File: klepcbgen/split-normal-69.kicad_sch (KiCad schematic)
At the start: 159 parts, among them J1 USB_B_Micro, J2 Conn_02x03_Odd_Even, K0 Esc, K1 !,1,,F1, K10 ),0,,F10, K11 _,-,,F11, K12 +,=,,F12, K13 Backspace, K14 Delete,Insert, K15 Tab, K16 Q, K17 W, K18 E, K19 R, K2 @,2,,F2, K20 T, K21 Y, K22 U, K23 I, K24 O, K25 P, K26 {,[, K27 },], K28 |,\, K29 ~~,`, K3 #,3,,F3, K30 Caps Lock, K31 A, K32 S, K33 D, K34 F, K35 G, K36 H, K37 J, K38 K, K39 L, K4 $,4,,F4, K40 :,;, K41 ",', K42 Enter, K43 Home,PgUp, K44 Shift, K45 Z, K46 X, K47 C, K48 V, K49 B, K5 %,5,,F5, K50 N, K51 M, K52 <,,, K53 >,., K54 ?,/, K55 Shift, K56 ↑, K57 End,PgDn, K58 Ctrl, K59 Win, K6 ^,6,,F6, K60 Alt, K61 Blank, K62 Blank, K63 Alt, K64 Fn, K65 Ctrl, K66 ←, K67 ↓, K68 →, K7 &,7,,F7, K8 *,8,,F8, K9 (,9,,F9, SW1 RESET_SW, U1 ATmega32U4-AU, Y1 Crystal

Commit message: update
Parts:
- H1, H2, H3, H4: footprint MountingHole:MountingHole_3.2mm_M3_DIN965 -> MountingHole:MountingHole_3.2mm_M3
- K61, K62: value Blank -> Space
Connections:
- net Col_0 renamed COL0
- net Col_1 renamed COL1
- net Col_10 renamed COL10
- net Col_11 renamed COL11
- net Col_12 renamed COL12
- net Col_13 renamed COL13
- net Col_14 renamed COL14
- net Col_15: no longer names the net of U1.40 (PF1)
- net Col_16: no longer names the net of U1.41 (PF0)
- net Col_17: no longer names the net of U1.1 (PE6)
- net Col_2 renamed COL2
- net Col_3 renamed COL3
- net Col_4 renamed COL4
- net Col_5 renamed COL5
- net Col_6 renamed COL6
- net Col_7 renamed COL7
- net Col_8 renamed COL8
- net Col_9 renamed COL9
- net Row_0 renamed ROW0
- net Row_1 renamed ROW1
- net Row_2 renamed ROW2
- net Row_3 renamed ROW3
- net Row_4 renamed ROW4
- net Row_5: no longer names the net of U1.27 (PD7)
- net Row_6: no longer names the net of U1.26 (PD6)
- no-connect marks 2 -> 7

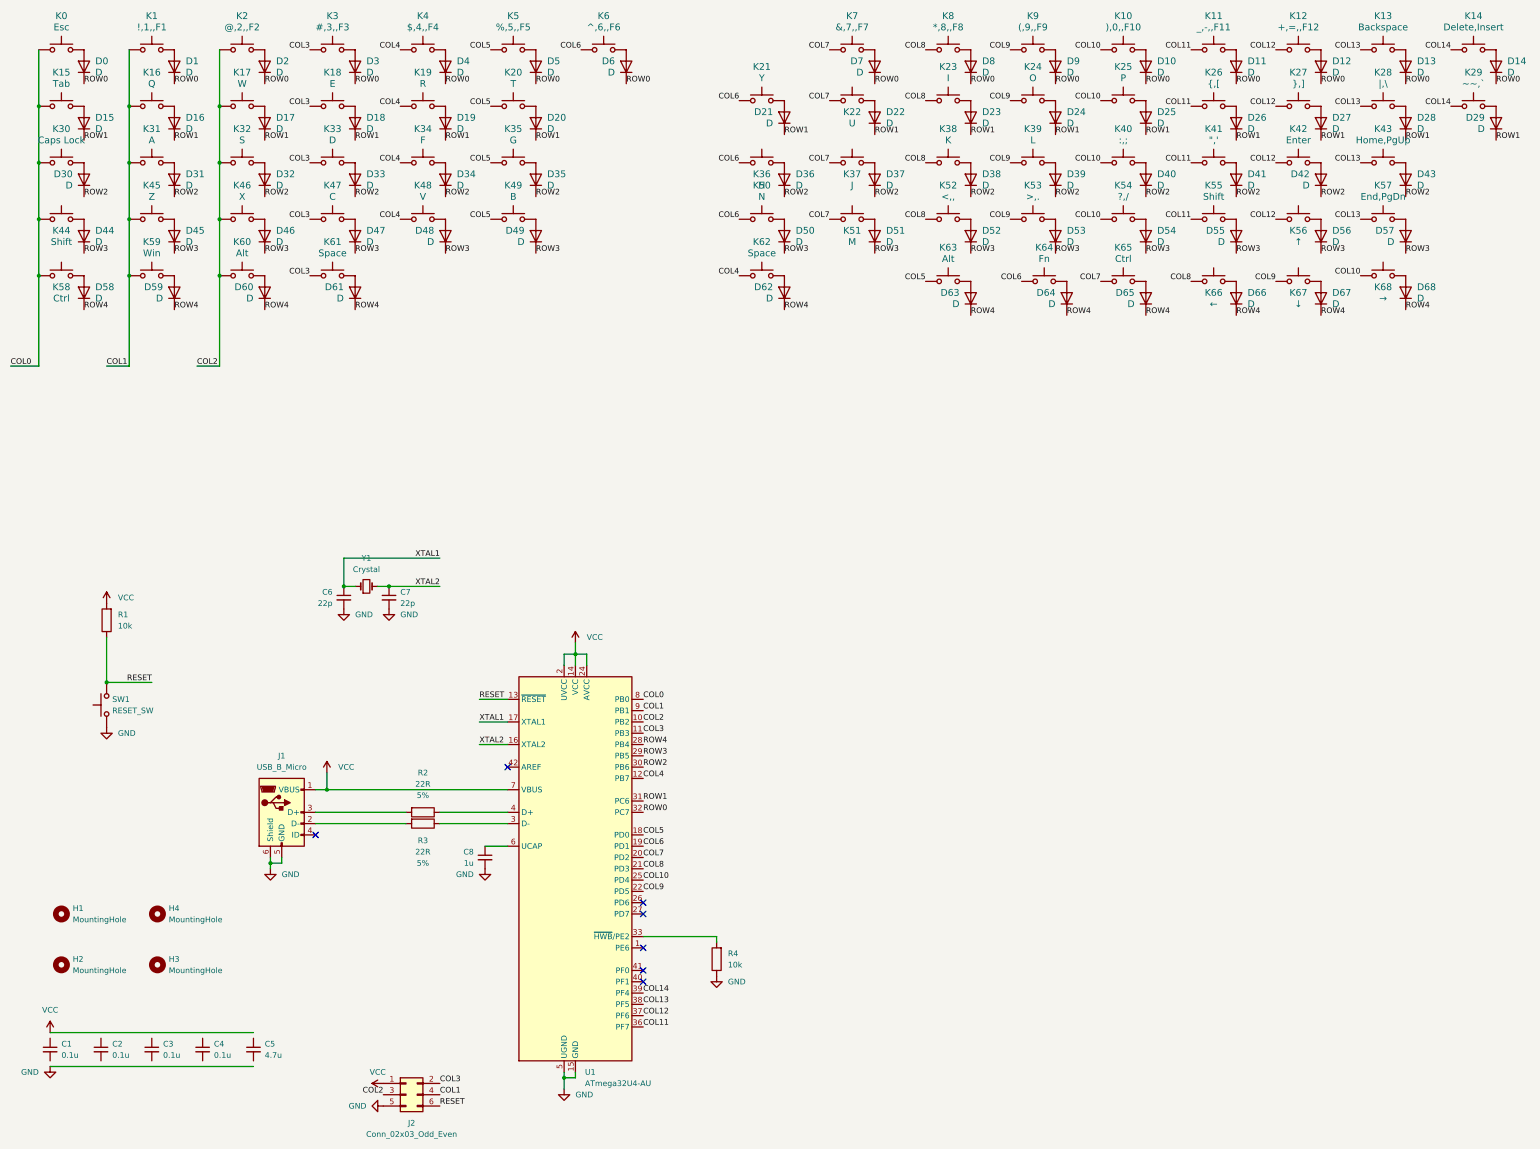
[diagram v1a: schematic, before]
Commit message: Continued development. Fixed the keyboard connections. Trying to figure out how to connect them together.
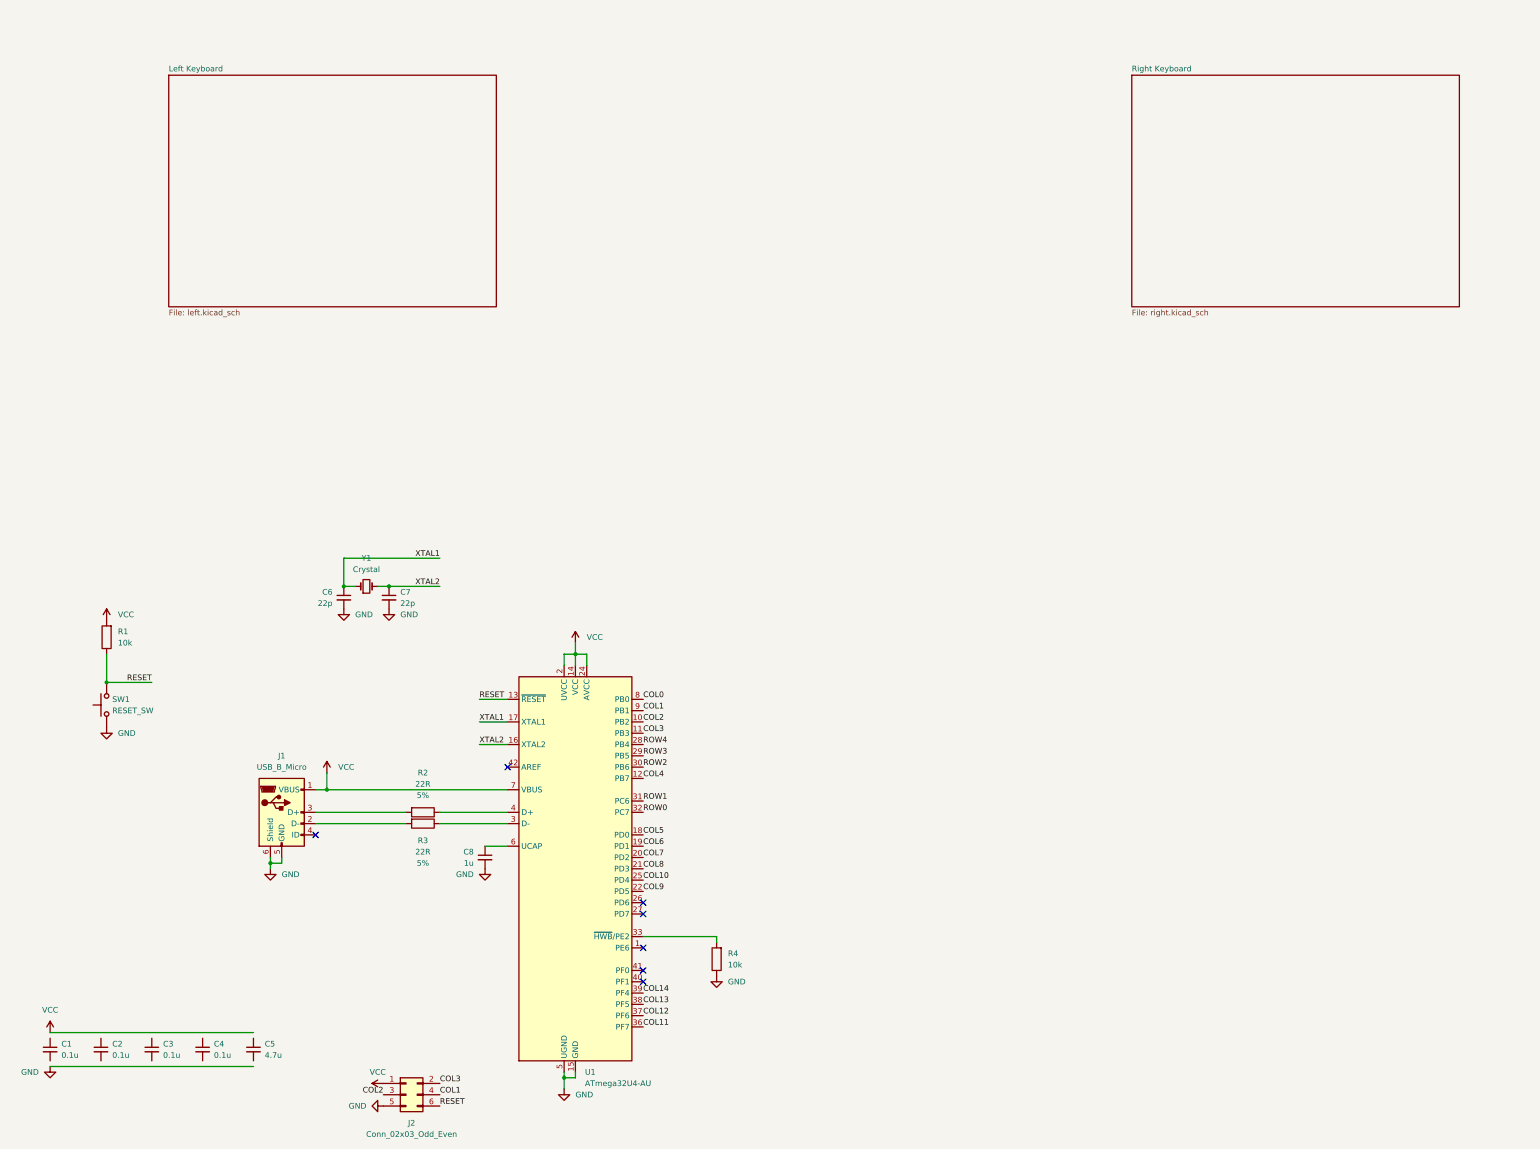
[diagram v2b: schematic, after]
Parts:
- removed D0, D1, D10, D11, D12, D13, D14, D15, D16, D17, D18, D19, D2, D20, D21, D22, D23, D24, D25, D26, D27, D28, D29, D3, D30, D31, D32, D33, D34, D35, D36, D37, D38, D39, D4, D40, D41, D42, D43, D44, D45, D46, D47, D48, D49, D5, D50, D51, D52, D53, D54, D55, D56, D57, D58, D59, D6, D60, D61, D62, D63, D64, D65, D66, D67, D68, D7, D8, D9: D, Diode_SMD:D_0805_2012Metric_Pad1.15x1.40mm_HandSolder, symbol Device:D
- removed H1, H2, H3, H4: MountingHole, MountingHole:MountingHole_3.2mm_M3, symbol Mechanical:MountingHole
- removed K0: Esc, Button_Switch_Keyboard:SW_Cherry_MX_1.00u_PCB, symbol Switch:SW_Push
- removed K1: !,1,,F1, Button_Switch_Keyboard:SW_Cherry_MX_1.00u_PCB, symbol Switch:SW_Push
- removed K10: ),0,,F10, Button_Switch_Keyboard:SW_Cherry_MX_1.00u_PCB, symbol Switch:SW_Push
- removed K11: _,-,,F11, Button_Switch_Keyboard:SW_Cherry_MX_1.00u_PCB, symbol Switch:SW_Push
- removed K12: +,=,,F12, Button_Switch_Keyboard:SW_Cherry_MX_1.00u_PCB, symbol Switch:SW_Push
- removed K13: Backspace, Button_Switch_Keyboard:SW_Cherry_MX_2.00u_PCB, symbol Switch:SW_Push
- removed K14: Delete,Insert, Button_Switch_Keyboard:SW_Cherry_MX_1.00u_PCB, symbol Switch:SW_Push
- removed K15: Tab, Button_Switch_Keyboard:SW_Cherry_MX_1.50u_PCB, symbol Switch:SW_Push
- removed K16: Q, Button_Switch_Keyboard:SW_Cherry_MX_1.00u_PCB, symbol Switch:SW_Push
- removed K17: W, Button_Switch_Keyboard:SW_Cherry_MX_1.00u_PCB, symbol Switch:SW_Push
- removed K18: E, Button_Switch_Keyboard:SW_Cherry_MX_1.00u_PCB, symbol Switch:SW_Push
- removed K19: R, Button_Switch_Keyboard:SW_Cherry_MX_1.00u_PCB, symbol Switch:SW_Push
- removed K2: @,2,,F2, Button_Switch_Keyboard:SW_Cherry_MX_1.00u_PCB, symbol Switch:SW_Push
- removed K20: T, Button_Switch_Keyboard:SW_Cherry_MX_1.00u_PCB, symbol Switch:SW_Push
- removed K21: Y, Button_Switch_Keyboard:SW_Cherry_MX_1.00u_PCB, symbol Switch:SW_Push
- removed K22: U, Button_Switch_Keyboard:SW_Cherry_MX_1.00u_PCB, symbol Switch:SW_Push
- removed K23: I, Button_Switch_Keyboard:SW_Cherry_MX_1.00u_PCB, symbol Switch:SW_Push
- removed K24: O, Button_Switch_Keyboard:SW_Cherry_MX_1.00u_PCB, symbol Switch:SW_Push
- removed K25: P, Button_Switch_Keyboard:SW_Cherry_MX_1.00u_PCB, symbol Switch:SW_Push
- removed K26: {,[, Button_Switch_Keyboard:SW_Cherry_MX_1.00u_PCB, symbol Switch:SW_Push
- removed K27: },], Button_Switch_Keyboard:SW_Cherry_MX_1.00u_PCB, symbol Switch:SW_Push
- removed K28: |,\, Button_Switch_Keyboard:SW_Cherry_MX_1.50u_PCB, symbol Switch:SW_Push
- removed K29: ~~,`, Button_Switch_Keyboard:SW_Cherry_MX_1.00u_PCB, symbol Switch:SW_Push
- removed K3: #,3,,F3, Button_Switch_Keyboard:SW_Cherry_MX_1.00u_PCB, symbol Switch:SW_Push
- removed K30: Caps Lock, Button_Switch_Keyboard:SW_Cherry_MX_1.75u_PCB, symbol Switch:SW_Push
- removed K31: A, Button_Switch_Keyboard:SW_Cherry_MX_1.00u_PCB, symbol Switch:SW_Push
- removed K32: S, Button_Switch_Keyboard:SW_Cherry_MX_1.00u_PCB, symbol Switch:SW_Push
- removed K33: D, Button_Switch_Keyboard:SW_Cherry_MX_1.00u_PCB, symbol Switch:SW_Push
- removed K34: F, Button_Switch_Keyboard:SW_Cherry_MX_1.00u_PCB, symbol Switch:SW_Push
- removed K35: G, Button_Switch_Keyboard:SW_Cherry_MX_1.00u_PCB, symbol Switch:SW_Push
- removed K36: H, Button_Switch_Keyboard:SW_Cherry_MX_1.00u_PCB, symbol Switch:SW_Push
- removed K37: J, Button_Switch_Keyboard:SW_Cherry_MX_1.00u_PCB, symbol Switch:SW_Push
- removed K38: K, Button_Switch_Keyboard:SW_Cherry_MX_1.00u_PCB, symbol Switch:SW_Push
- removed K39: L, Button_Switch_Keyboard:SW_Cherry_MX_1.00u_PCB, symbol Switch:SW_Push
- removed K4: $,4,,F4, Button_Switch_Keyboard:SW_Cherry_MX_1.00u_PCB, symbol Switch:SW_Push
- removed K40: :,;, Button_Switch_Keyboard:SW_Cherry_MX_1.00u_PCB, symbol Switch:SW_Push
- removed K41: ",', Button_Switch_Keyboard:SW_Cherry_MX_1.00u_PCB, symbol Switch:SW_Push
- removed K42: Enter, Button_Switch_Keyboard:SW_Cherry_MX_2.25u_PCB, symbol Switch:SW_Push
- removed K43: Home,PgUp, Button_Switch_Keyboard:SW_Cherry_MX_1.00u_PCB, symbol Switch:SW_Push
- removed K44: Shift, Button_Switch_Keyboard:SW_Cherry_MX_2.25u_PCB, symbol Switch:SW_Push
- removed K45: Z, Button_Switch_Keyboard:SW_Cherry_MX_1.00u_PCB, symbol Switch:SW_Push
- removed K46: X, Button_Switch_Keyboard:SW_Cherry_MX_1.00u_PCB, symbol Switch:SW_Push
- removed K47: C, Button_Switch_Keyboard:SW_Cherry_MX_1.00u_PCB, symbol Switch:SW_Push
- removed K48: V, Button_Switch_Keyboard:SW_Cherry_MX_1.00u_PCB, symbol Switch:SW_Push
- removed K49: B, Button_Switch_Keyboard:SW_Cherry_MX_1.00u_PCB, symbol Switch:SW_Push
- removed K5: %,5,,F5, Button_Switch_Keyboard:SW_Cherry_MX_1.00u_PCB, symbol Switch:SW_Push
- removed K50: N, Button_Switch_Keyboard:SW_Cherry_MX_1.00u_PCB, symbol Switch:SW_Push
- removed K51: M, Button_Switch_Keyboard:SW_Cherry_MX_1.00u_PCB, symbol Switch:SW_Push
- removed K52: <,,, Button_Switch_Keyboard:SW_Cherry_MX_1.00u_PCB, symbol Switch:SW_Push
- removed K53: >,., Button_Switch_Keyboard:SW_Cherry_MX_1.00u_PCB, symbol Switch:SW_Push
- removed K54: ?,/, Button_Switch_Keyboard:SW_Cherry_MX_1.00u_PCB, symbol Switch:SW_Push
- removed K55: Shift, Button_Switch_Keyboard:SW_Cherry_MX_1.75u_PCB, symbol Switch:SW_Push
- removed K56: ↑, Button_Switch_Keyboard:SW_Cherry_MX_1.00u_PCB, symbol Switch:SW_Push
- removed K57: End,PgDn, Button_Switch_Keyboard:SW_Cherry_MX_1.00u_PCB, symbol Switch:SW_Push
- removed K58: Ctrl, Button_Switch_Keyboard:SW_Cherry_MX_1.25u_PCB, symbol Switch:SW_Push
- removed K59: Win, Button_Switch_Keyboard:SW_Cherry_MX_1.25u_PCB, symbol Switch:SW_Push
- removed K6: ^,6,,F6, Button_Switch_Keyboard:SW_Cherry_MX_1.00u_PCB, symbol Switch:SW_Push
- removed K60: Alt, Button_Switch_Keyboard:SW_Cherry_MX_1.25u_PCB, symbol Switch:SW_Push
- removed K61, K62: Space, Button_Switch_Keyboard:SW_Cherry_MX_2.75u_PCB, symbol Switch:SW_Push
- removed K63: Alt, Button_Switch_Keyboard:SW_Cherry_MX_1.00u_PCB, symbol Switch:SW_Push
- removed K64: Fn, Button_Switch_Keyboard:SW_Cherry_MX_1.00u_PCB, symbol Switch:SW_Push
- removed K65: Ctrl, Button_Switch_Keyboard:SW_Cherry_MX_1.00u_PCB, symbol Switch:SW_Push
- removed K66: ←, Button_Switch_Keyboard:SW_Cherry_MX_1.00u_PCB, symbol Switch:SW_Push
- removed K67: ↓, Button_Switch_Keyboard:SW_Cherry_MX_1.00u_PCB, symbol Switch:SW_Push
- removed K68: →, Button_Switch_Keyboard:SW_Cherry_MX_1.00u_PCB, symbol Switch:SW_Push
- removed K7: &,7,,F7, Button_Switch_Keyboard:SW_Cherry_MX_1.00u_PCB, symbol Switch:SW_Push
- removed K8: *,8,,F8, Button_Switch_Keyboard:SW_Cherry_MX_1.00u_PCB, symbol Switch:SW_Push
- removed K9: (,9,,F9, Button_Switch_Keyboard:SW_Cherry_MX_1.00u_PCB, symbol Switch:SW_Push
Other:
- added sheet Left Keyboard (left.kicad_sch)
- added sheet Right Keyboard (right.kicad_sch)
- moved on the sheet: R1

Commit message: Moved things around more so that they make sense. Slowly figuring it out.
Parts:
- removed C1, C2, C3, C4: 0.1u, Capacitor_SMD:C_0805_2012Metric_Pad1.15x1.40mm_HandSolder, symbol Device:C_Small
- removed C5: 4.7u, Capacitor_SMD:C_0805_2012Metric_Pad1.15x1.40mm_HandSolder, symbol Device:C_Small
- removed C6, C7: 22p, Capacitor_SMD:C_0805_2012Metric_Pad1.15x1.40mm_HandSolder, symbol Device:C_Small
- removed C8: 1u, Capacitor_SMD:C_0805_2012Metric_Pad1.15x1.40mm_HandSolder, symbol Device:C_Small
- removed J1: USB_B_Micro, Connector_USB:USB_Micro-B_Wuerth_629105150521_CircularHoles, symbol Connector:USB_B_Micro
- removed J2: Conn_02x03_Odd_Even, Connector_PinHeader_2.54mm:PinHeader_2x03_P2.54mm_Vertical, symbol Connector_Generic:Conn_02x03_Odd_Even
- removed R1, R4: 10k, Resistor_SMD:R_0805_2012Metric_Pad1.15x1.40mm_HandSolder, symbol Device:R
- removed R2, R3: 22R, Resistor_SMD:R_0805_2012Metric_Pad1.15x1.40mm_HandSolder, symbol Device:R
- removed SW1: RESET_SW, Button_Switch_SMD:SW_Push_1P1T_NO_6x6mm_H9.5mm, symbol Switch:SW_Push
- removed U1: ATmega32U4-AU, Package_QFP:TQFP-44_10x10mm_P0.8mm, symbol MCU_Microchip_ATmega:ATmega32U4-A
- removed Y1: Crystal, Crystal:Crystal_SMD_5032-2Pin_5.0x3.2mm_HandSoldering, symbol Device:Crystal_Small
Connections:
- no-connect marks 7 -> 0
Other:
- sheet Left Keyboard ports: added {COMMON_ROWS}, {LEFT_COLUMNS}, {RIGHT_COLUMNS}; removed none

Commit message: Continuing.
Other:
- sheet Left Keyboard ports: added none; removed {COMMON_ROWS}, {LEFT_COLUMNS}, {RIGHT_COLUMNS}
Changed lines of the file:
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@@
 	(title_block
 		(title "Split Normal 69")
-		(date "2025-05-13 17:42")
-		(comment 1 "Author: Yiannis Michael")
-		(comment 2 "Generated by klepcbgen.py v0.1")
+		(date "2025-06-11")
 	)
 	(sheet
-		(at 271.145 41.91)
+		(at 263.525 66.675)
 		(size 73.66 144.145)
 		(exclude_from_sim no)
@@
 		)
 		(property "Sheetname" "Right Keyboard"
-			(at 271.145 41.1984 0)
+			(at 263.525 65.9634 0)
 			(effects
 				(font
@@
 		)
 		(property "Sheetfile" "right.kicad_sch"
-			(at 271.145 186.6396 0)
+			(at 263.525 211.4046 0)
 			(effects
 				(font
@@
 	)
 	(sheet
-		(at 99.06 41.275)
+		(at 91.44 66.04)
 		(size 73.66 144.78)
 		(exclude_from_sim no)
@@
 		)
 		(property "Sheetname" "Left Keyboard"
-			(at 99.06 40.5634 0)
+			(at 91.44 65.3284 0)
 			(effects
 				(font
@@
 		)
 		(property "Sheetfile" "left.kicad_sch"
-			(at 99.06 186.6396 0)
+			(at 91.44 211.4046 0)
 			(effects
 				(font
@@
 			)
 		)
-		(pin "{LEFT_COLUMNS}" bidirectional
-			(at 172.72 47.625 0)
-			(effects
-				(font
-					(size 1.27 1.27)
-				)
-				(justify right)
-			)
-		)
-		(pin "{COMMON_ROWS}" bidirectional
-			(at 172.72 52.705 0)
-			(effects
-				(font
-					(size 1.27 1.27)
-				)
-				(justify right)
-			)
-		)
-		(pin "{RIGHT_COLUMNS}" bidirectional
-			(at 172.72 57.785 0)
-			(effects
-				(font
-					(size 1.27 1.27)
-				)
-				(justify right)
-			)
-		)
